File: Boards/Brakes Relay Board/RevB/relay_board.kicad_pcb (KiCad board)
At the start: 2 copper layers, 85 x 56 mm, 38 parts, among them J1 Screw_Terminal_01x04, J2 Screw_Terminal_01x04, J3 Screw_Terminal_01x04, J4 Screw_Terminal_01x04, J5 Conn_02x10_Counter_Clockwise, J6 Conn_02x12_Counter_Clockwise, J7 Screw_Terminal_01x04, U1 ALQ105, U2 ALQ105, U4 ALQ105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

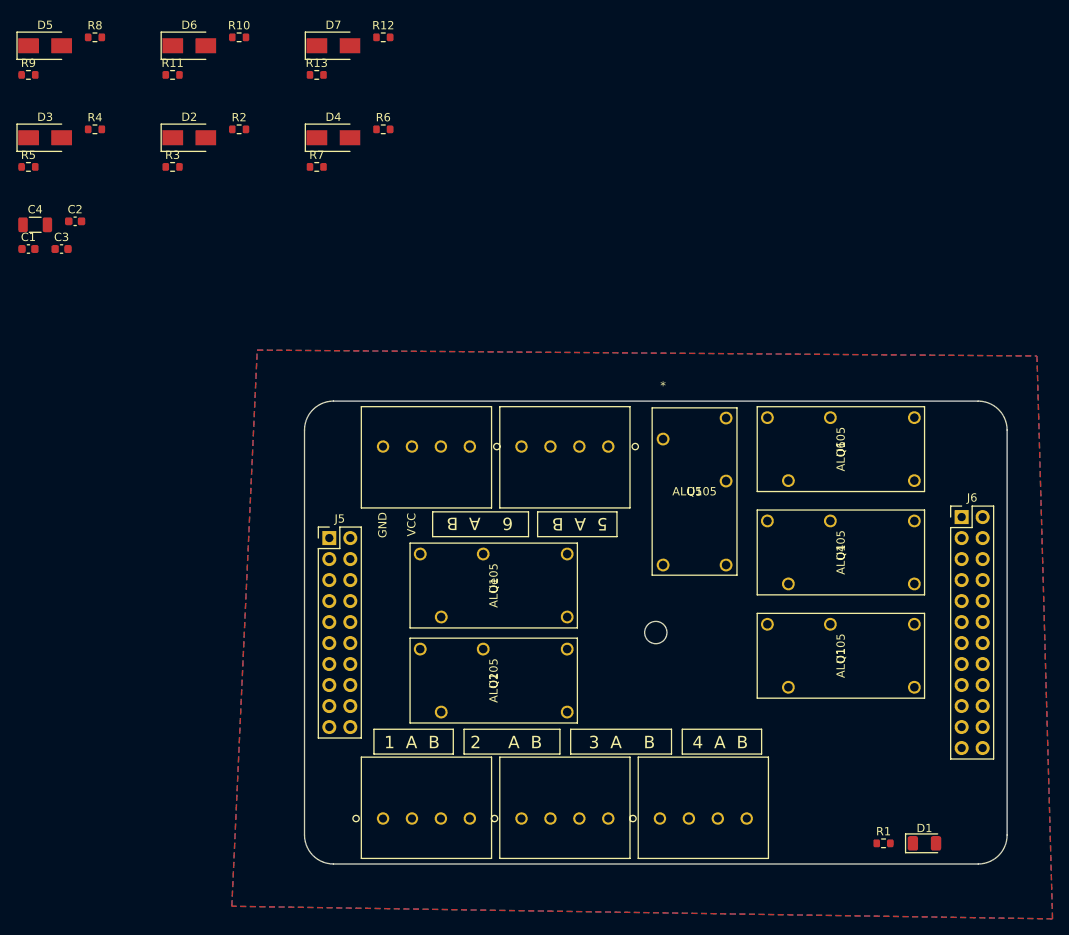
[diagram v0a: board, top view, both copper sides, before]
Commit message: Added new components to PCB
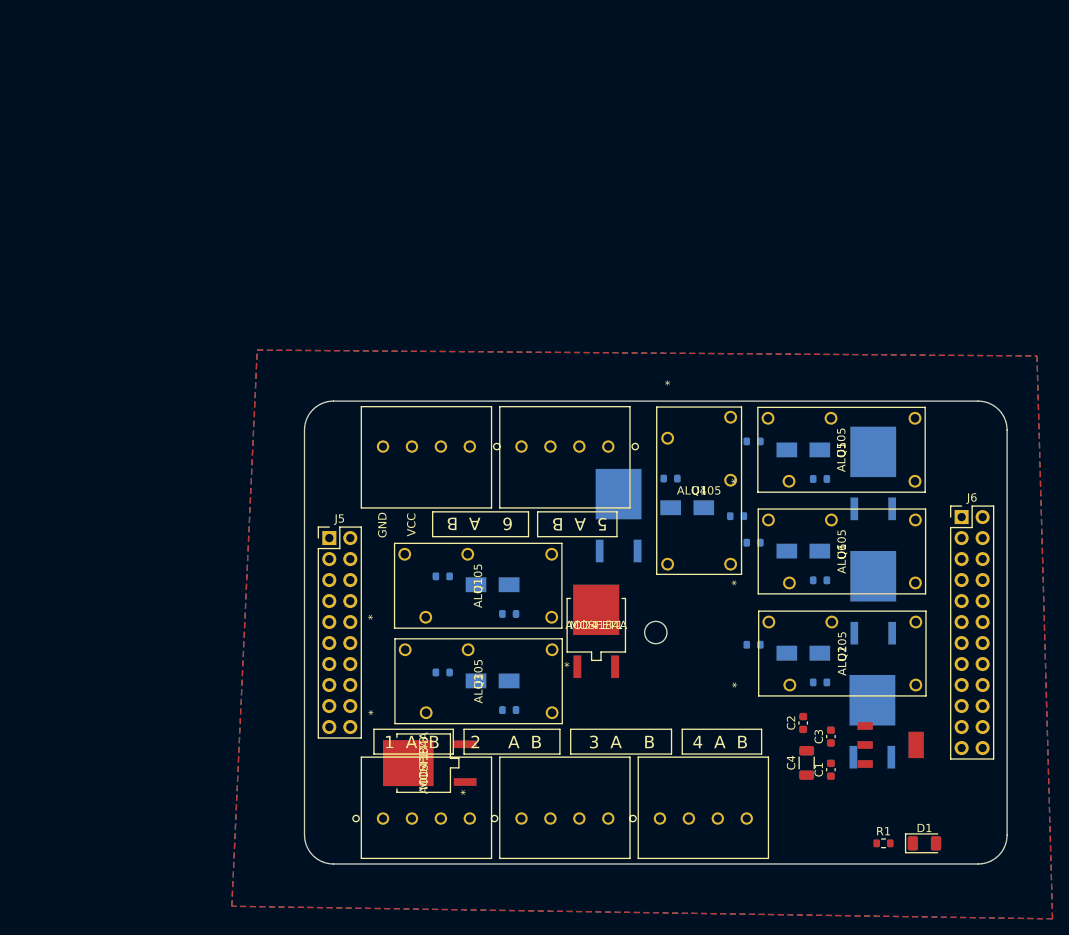
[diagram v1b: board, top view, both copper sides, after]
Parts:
- removed Ue: ALQ105, ALQ105-BAJA-FP:ALQ105
- added MOSFET1: AOD4184A, BAJA_AOD:AOD4184A, F.Cu at (195.3, 97.1)
- added MOSFET2: AOD4184A, BAJA_AOD:AOD4184A, B.Cu at (228.7, 108.1)
- added MOSFET3: AOD4184A, BAJA_AOD:AOD4184A, F.Cu at (174.4, 113.8)
- added MOSFET4: AOD4184A, BAJA_AOD:AOD4184A, B.Cu at (198.0, 83.1)
- added MOSFET5: AOD4184A, BAJA_AOD:AOD4184A, B.Cu at (228.8, 78.0)
- added MOSFET6: AOD4184A, BAJA_AOD:AOD4184A, B.Cu at (228.8, 93.1)
- added U3: ALQ105, ALQ105-BAJA-FP:ALQ105, F.Cu at (172.2, 100.1)
- added VR1: ~, LM1117IMPX-5:SOT230P700X180-4N, F.Cu at (230.9, 111.6)
- D2, D3, D4, D5, D6, D7, R10, R11, R12, R13, R2, R3, R4, R5, R6, R7, R8, R9: moved to B.Cu
- moved C1 115.7 mm to (223.7, 114.6), turned to 90 degrees
- moved R5 114.3 mm to (222.4, 104.0), turned to 180 degrees
- moved C4 113.8 mm to (220.8, 113.8), turned to 90 degrees
- moved D3 110.9 mm to (220.3, 100.5), turned to 180 degrees
- moved C3 110.2 mm to (223.7, 110.6), turned to 90 degrees
- moved C2 107.0 mm to (220.3, 108.9), turned to 90 degrees
- moved R4 101.2 mm to (214.3, 99.5), turned to 180 degrees
- moved R8 96.9 mm to (212.3, 83.9)
- moved D5 95.7 mm to (206.3, 82.9)
- moved R11 92.3 mm to (222.4, 79.4), turned to 180 degrees
- moved R9 91.8 mm to (204.3, 79.4)
- moved D6 88.9 mm to (220.3, 75.9), turned to 180 degrees
- moved R13 86.3 mm to (222.4, 91.7), turned to 180 degrees
- moved D7 83.5 mm to (220.3, 88.2), turned to 180 degrees
- moved R10 79.1 mm to (214.3, 74.9), turned to 180 degrees
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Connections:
- U1 pad 1: /Ch1A -> /Relay_1/A
- U1 pad 3: /R0 -> Net-(D2-Pad1)
- U1 pad 4: /GND -> +5V
- U2 pad 1: /Ch4A -> /Ch2A
- U2 pad 2: /Ch4 -> /Ch2
- U2 pad 3: /R3 -> Net-(D3-Pad1)
- U2 pad 4: /GND -> +5V
- U2 pad 5: /Ch4B -> /Ch2B
- U4 pad 1: /Ch5A -> /Ch4A
- U4 pad 2: /Ch5 -> /Ch4
- U4 pad 3: /R4 -> Net-(D5-Pad1)
- U4 pad 4: /GND -> +5V
- U4 pad 5: /Ch5B -> /Ch4B
- U5 pad 1: /Ch3A -> /Ch5A
- U5 pad 2: /Ch3 -> /Ch5
- U5 pad 3: /R2 -> Net-(D6-Pad1)
- U5 pad 4: /GND -> +5V
- U5 pad 5: /Ch3B -> /Ch5B
- U6 pad 3: /R5 -> Net-(D7-Pad1)
- U6 pad 4: /GND -> +5V

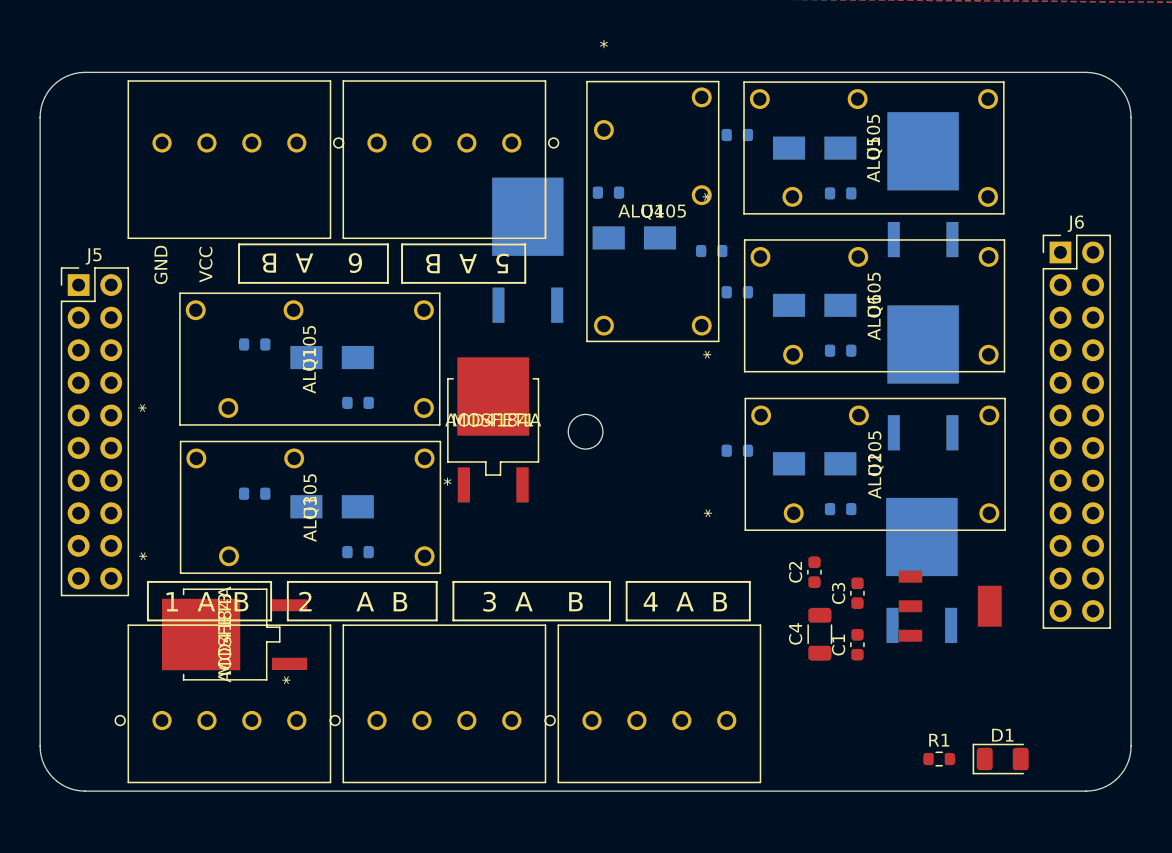
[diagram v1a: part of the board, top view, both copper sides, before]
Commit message: Routed relay board rev b
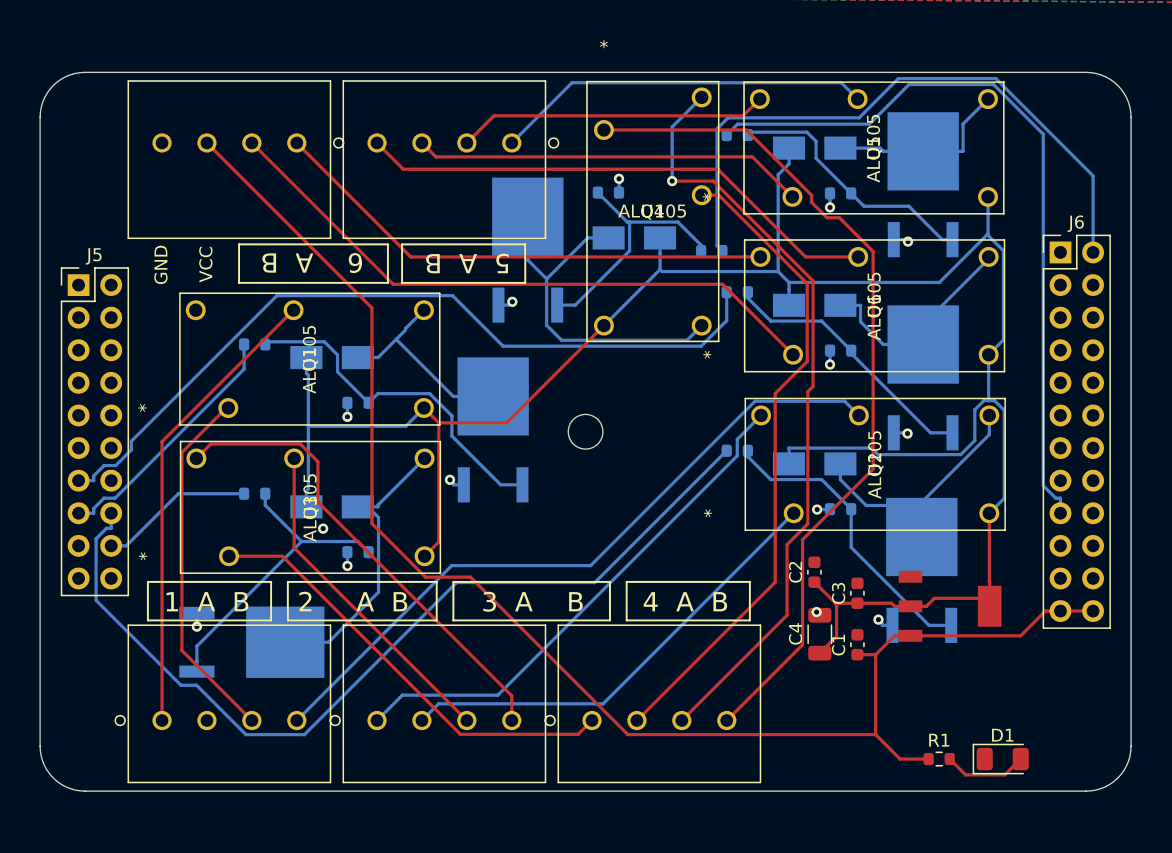
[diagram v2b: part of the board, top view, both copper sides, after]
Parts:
- MOSFET1, MOSFET3: moved to B.Cu
- moved MOSFET3 2.88 mm to (177.2, 114.4)
- turned MOSFET1 to 180 degrees
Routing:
- net +5V: track 0.00 -> 171.2 mm
- net /VCC: track 0.00 -> 111.9 mm
- net /R1: track 0.00 -> 70.1 mm
- net /Ch4B: track 0.00 -> 66.5 mm
- net /R5: track 0.00 -> 61.7 mm
- net /Ch4A: track 0.00 -> 60.2 mm, vias 0 -> 1
- net /R4: track 0.00 -> 58.2 mm
- net /Ch2: track 0.00 -> 54.6 mm
- net /Ch4: track 0.00 -> 50.6 mm
- net /R3: track 0.00 -> 49.7 mm
- net /Ch6B: track 0.00 -> 49.0 mm
- net /Ch6: track 0.00 -> 41.2 mm
- net /Ch2A: track 0.00 -> 40.5 mm
- net /Ch6A: track 0.00 -> 39.8 mm
- net /Ch3A: track 0.00 -> 36.9 mm
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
